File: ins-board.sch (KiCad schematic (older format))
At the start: 54 parts, among them P1 PWR, U1 STM32F042C6T6, U2 MIC5201-3.3YS, U3 MAX3051, U4 H3LIS331DL, U5 MPU6000, U6 HMC5883L, U7 MS5611-01BA, X1 CRYSTAL 16MHz 10ppm

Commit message: component values
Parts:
- removed C1, C4: 1uF, symbol C
- removed C6: 0.1uF, symbol C
- added R10, R11, R9: 10k, symbol R
- added R12: 0R, symbol R
- C12: renamed from C15; value C -> 1uF
- C16: renamed from C19; value C -> 0.1uF
- C17: renamed from C20; value C -> 10uF
- C8: renamed from C11; value C -> 0.1uF
- R1: value R -> 15k
- R2: value R -> 10k
- renumbered C2 to C1, C13 to C10, C14 to C11, C16 to C13, C17 to C14, C18 to C15, C21 to C18, C22 to C19, C3 to C2, C23 to C20, C24 to C21, C25 to C22, C26 to C23, C27 to C24, C28 to C25, C29 to C26, C5 to C3, C7 to C4, C8 to C5, C9 to C6, C10 to C7, C12 to C9, R9 to R13
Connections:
- net labels added: CAN_EN
- wire segments 126 -> 134
- no-connect marks 7 -> 8
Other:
- moved on the sheet: P1

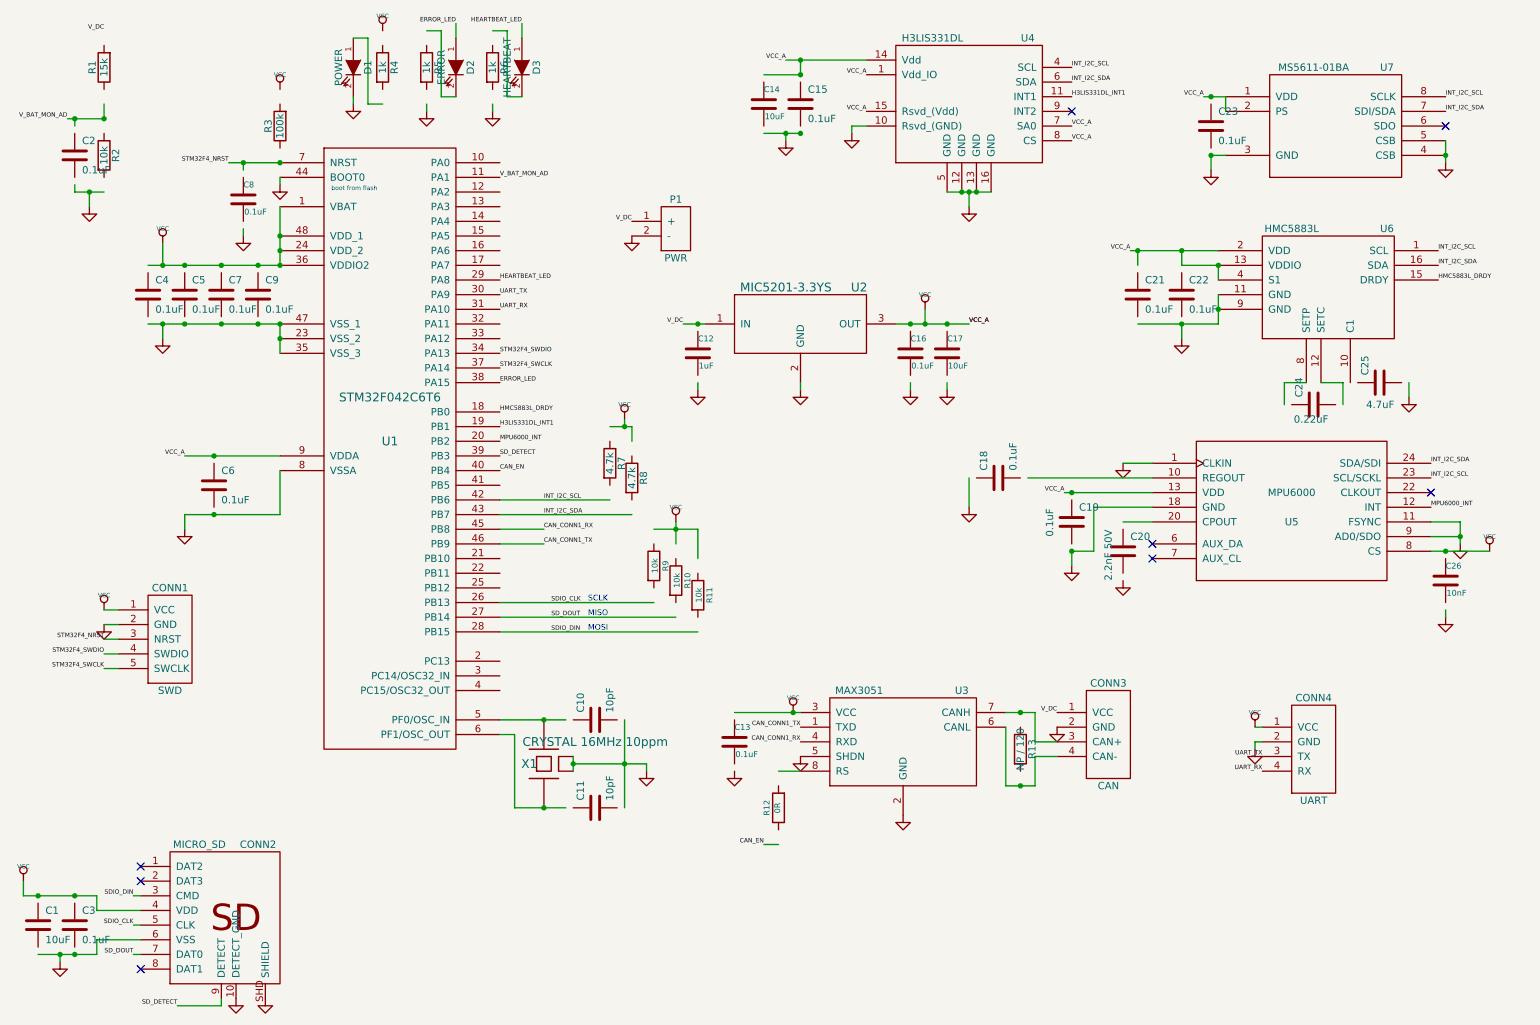
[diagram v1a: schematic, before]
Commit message: sd-card fix
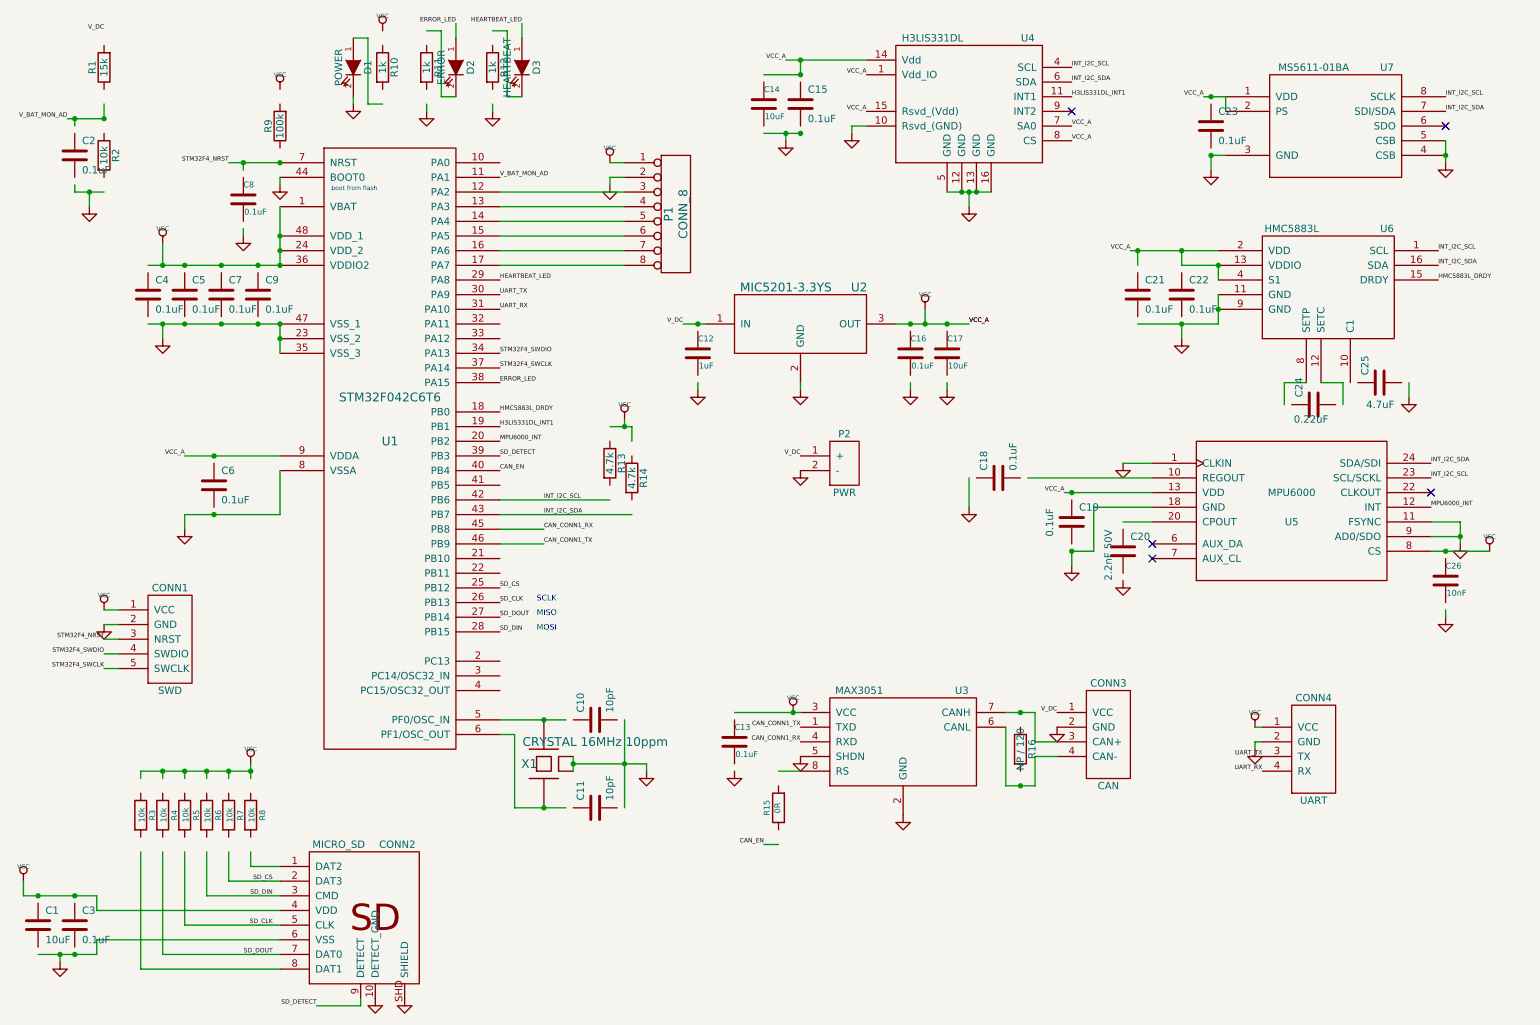
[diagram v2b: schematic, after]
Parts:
- added P1: CONN_8, symbol CONN_8
- added R6, R7, R8: 10k, symbol R
- renumbered P1 to P2, R4 to R10, R5 to R11, R6 to R12, R7 to R13, R8 to R14, R12 to R15, R13 to R16, R9 to R3, R10 to R4, R11 to R5, R3 to R9
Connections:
- net labels added: SD_CLK, SD_CS, SD_DIN
- net labels removed: SDIO_CLK, SDIO_DIN
- wire segments 134 -> 153
- no-connect marks 8 -> 5
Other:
- moved on the sheet: CONN2, P2, R3, R4, R5

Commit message: remove optional components
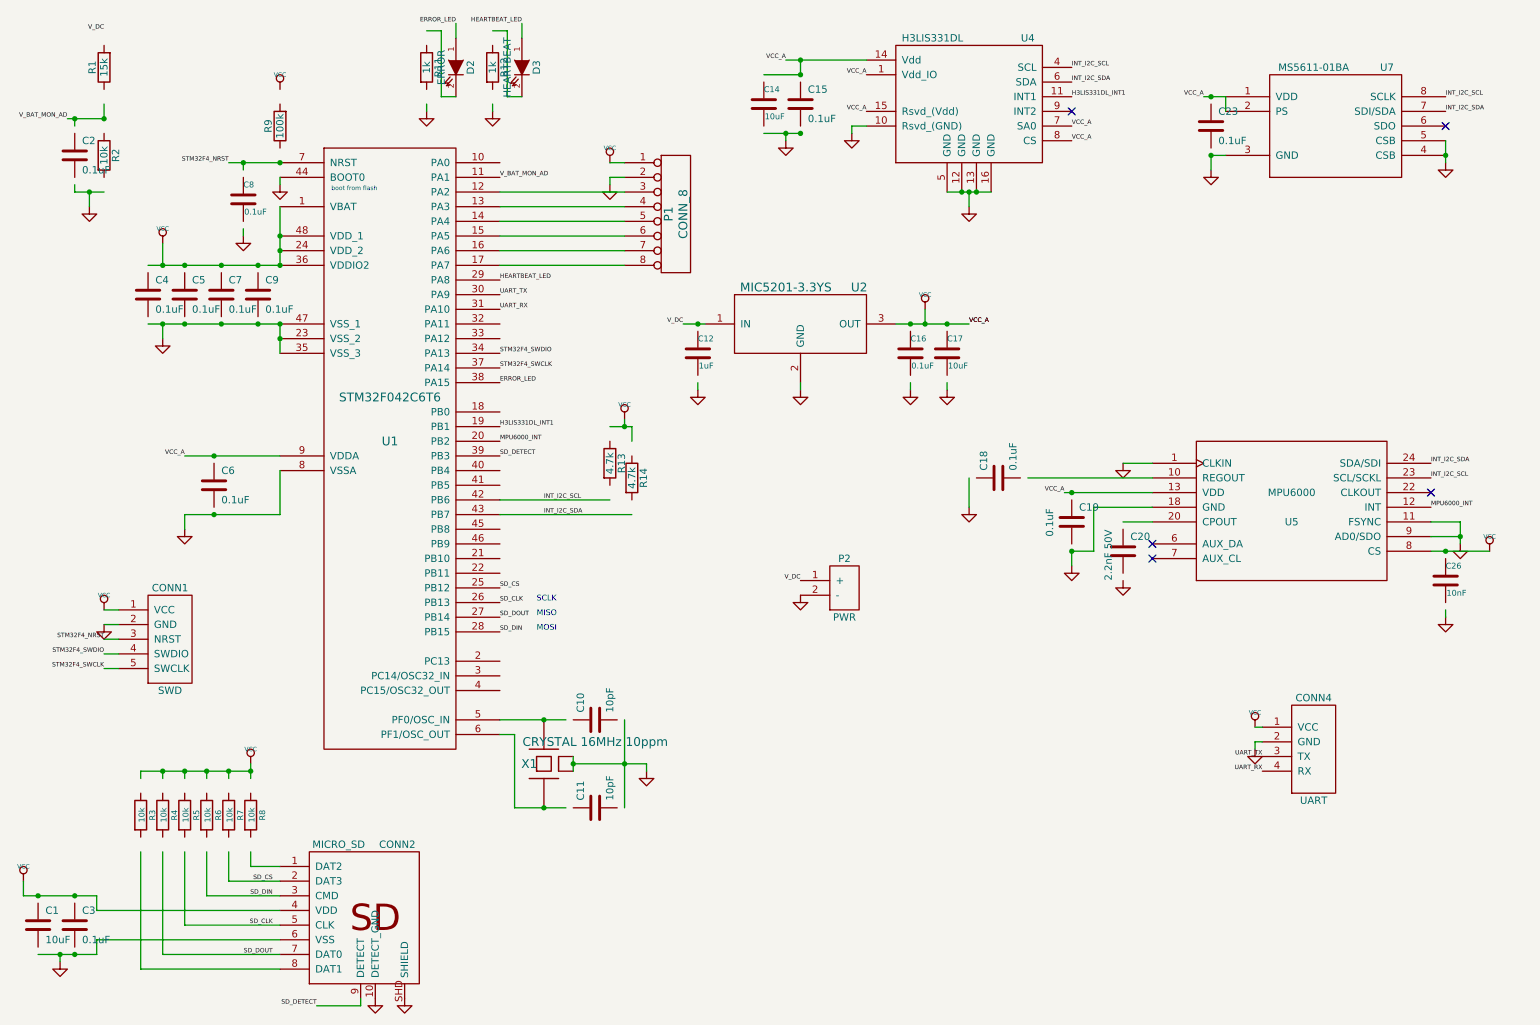
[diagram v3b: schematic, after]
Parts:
- removed C13: 0.1uF, ~, symbol C
- removed C21, C22: 0.1uF, symbol C
- removed C24: 0.22uF, symbol C
- removed C25: 4.7uF, symbol C
- removed CONN3: CAN, MODULE, symbol CAN
- removed D1: POWER, symbol LED
- removed R10: 1k, symbol R
- removed R15: 0R, symbol R
- removed R16: NP / 120, symbol R
- removed U3: MAX3051, MODULE, symbol MAX3051
- removed U6: HMC5883L, MODULE, symbol HMC5883L
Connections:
- net labels removed: CAN_CONN1_RX, CAN_CONN1_TX, CAN_EN, HMC5883L_DRDY
- wire segments 153 -> 124
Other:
- moved on the sheet: P2

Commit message: references
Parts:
- renumbered C14 to C13, C15 to C14, C16 to C15, C17 to C16, C18 to C17, C19 to C18, C20 to C19, C23 to C20, C26 to C21, CONN4 to CONN3, D2 to D1, D3 to D2, R11 to R10, R12 to R11, R13 to R12, R14 to R13, U4 to U3, U5 to U4, U7 to U5

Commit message: pcb + footprints
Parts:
- C1, C10, C11, C12, C14, C15, C16, C17, C18, C19, C2, C20, C21, C3, C4, C5, C6, C7, C8, C9, D1, D2, R1, R10, R11, R12, R13, R2, R3, R4, R5, R6, R7, R8, R9: footprint (none) -> _std:_0603-W
- C13: footprint ~ -> _std:_0603-W
- CONN1: footprint MODULE -> _connectors:_Pin2mm_5z
- CONN2: footprint MODULE -> _div:_Molex-microSD-502570-0893
- CONN3: footprint MODULE -> _connectors:_Molex-PicoBlade-SMD-4
- P1: footprint (none) -> _connectors:_Solder_Pad1.27_8
- P2: footprint MODULE -> _connectors:_Molex-PicoBlade-SMD-2
- U1: footprint MODULE -> _lqfp:_LQFP48
- U2: footprint (none) -> _std:_SOT23-3
- U3: footprint MODULE -> _sensors:_H3LIS331DL
- U4: footprint MODULE -> _sensors:_MPU-60X0
- U5: footprint MODULE -> _sensors:_MS5611-01BA
- X1: footprint (none) -> _div:_TSX-3225-SMD-XTAL

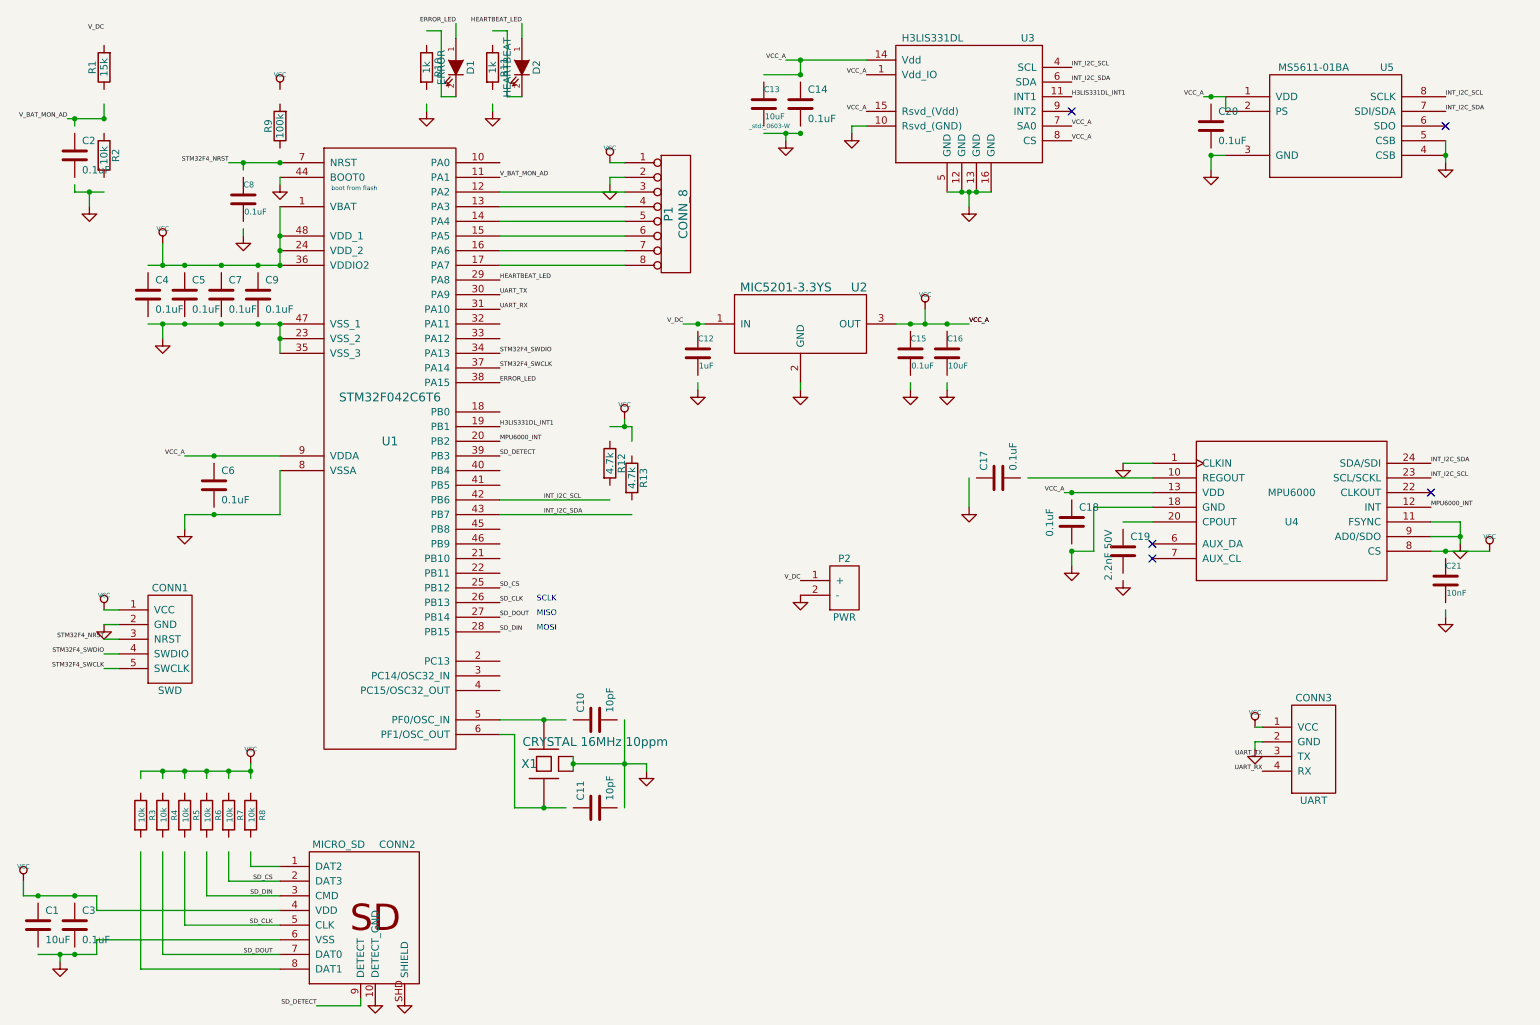
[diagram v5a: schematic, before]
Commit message: Add pressure sensor (sch) & fix drc violations
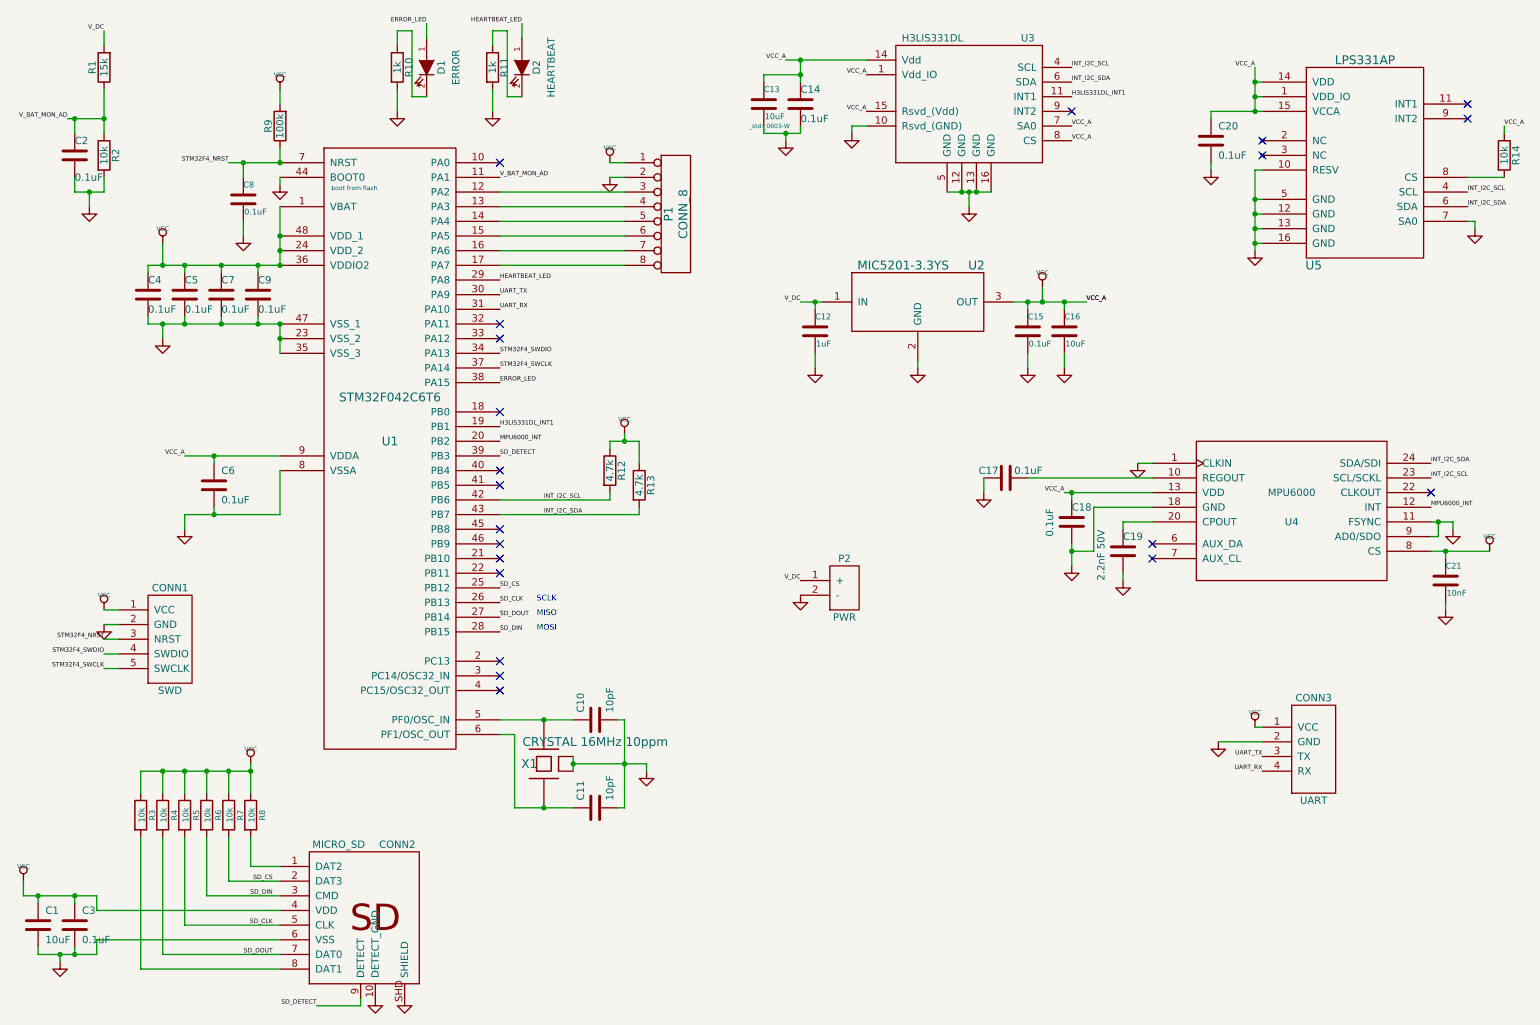
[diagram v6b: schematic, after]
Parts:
- removed U5: MS5611-01BA, _sensors:_MS5611-01BA, symbol MS5611-01BA
- added R14: 10k, symbol R
- added U5: LPS331AP, symbol LPS331AP
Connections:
- wire segments 124 -> 222
- no-connect marks 5 -> 21
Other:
- moved on the sheet: C12, C15, C16, C17, C20, D1, R10, R12, R13, U2
